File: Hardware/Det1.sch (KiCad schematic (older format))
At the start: 11 parts

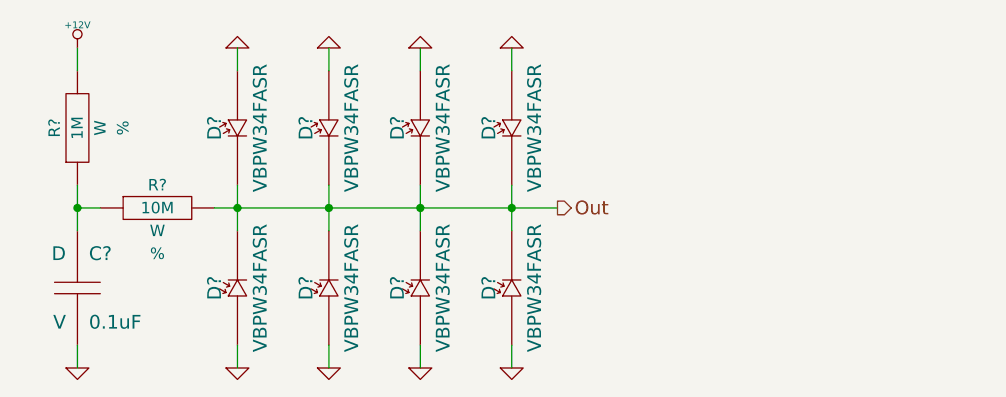
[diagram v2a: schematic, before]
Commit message: Fill BOM fields for detector section
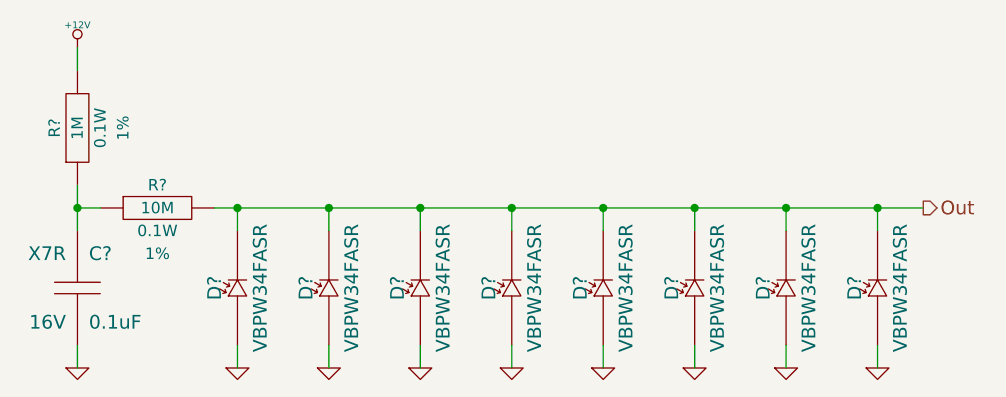
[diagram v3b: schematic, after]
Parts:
- removed C?: 0.1uF, ~, symbol C
- removed D? (x8): VBPW34FASR, ~, symbol DIODE-PHOTO
- removed R?: 10M, ~, symbol R
- added C?: 0.1uF, CAPC1608, symbol C
- added D? (x8): VBPW34FASR, DIOC-BPW34R, symbol DIODE-PHOTO
- added R?: 10M, RESC1608, symbol R
- R?: footprint ~ -> RESC1608; Distributor Part No (none) -> 311-1.00MHRCT-ND; MFR Name (none) -> Yageo; MFR Part No (none) -> RC0603FR-071ML; Power W -> 0.1W; Tolerance % -> 1%
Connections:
- net GND: now also C?.2, D?.1, D?.1, D?.1, D?.1, D?.1, D?.1, D?.1, D?.1
- net Out: now also D?.2, D?.2, D?.2, D?.2, D?.2, D?.2, D?.2, D?.2, R?.2
- net at R?.1: now also C?.1, R?.1

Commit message: Initial annotation
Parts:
- gave numbers to parts that had none: 11
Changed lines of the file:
@@
 $EndDescr
 $Comp
-L GND #PWR?
+L GND #PWR3
 U 1 1 523D026F
 P 3800 3700
-F 0 "#PWR?" H 3800 3700 30  0001 C CNN
+F 0 "#PWR3" H 3800 3700 30  0001 C CNN
 F 1 "GND" H 3800 3630 30  0001 C CNN
 F 2 "" H 3800 3700 60  0000 C CNN
@@
 $EndComp
 $Comp
-L GND #PWR?
+L GND #PWR4
 U 1 1 523D027E
 P 4200 3700
-F 0 "#PWR?" H 4200 3700 30  0001 C CNN
+F 0 "#PWR4" H 4200 3700 30  0001 C CNN
 F 1 "GND" H 4200 3630 30  0001 C CNN
 F 2 "" H 4200 3700 60  0000 C CNN
@@
 $EndComp
 $Comp
-L GND #PWR?
+L GND #PWR6
 U 1 1 523D029C
 P 5000 3700
-F 0 "#PWR?" H 5000 3700 30  0001 C CNN
+F 0 "#PWR6" H 5000 3700 30  0001 C CNN
 F 1 "GND" H 5000 3630 30  0001 C CNN
 F 2 "" H 5000 3700 60  0000 C CNN
@@
 $EndComp
 $Comp
-L GND #PWR?
+L GND #PWR5
 U 1 1 523D02AB
 P 4600 3700
-F 0 "#PWR?" H 4600 3700 30  0001 C CNN
+F 0 "#PWR5" H 4600 3700 30  0001 C CNN
 F 1 "GND" H 4600 3630 30  0001 C CNN
 F 2 "" H 4600 3700 60  0000 C CNN
@@
 Out
 $Comp
-L +12V #PWR?
+L +12V #PWR1
 U 1 1 523D1D05
 P 3100 2300
-F 0 "#PWR?" H 3100 2250 20  0001 C CNN
+F 0 "#PWR1" H 3100 2250 20  0001 C CNN
 F 1 "+12V" H 3100 2400 30  0000 C CNN
 F 2 "" H 3100 2300 60  0000 C CNN
@@
 $EndComp
 $Comp
-L R R?
+L R R1
 U 1 1 523D1D2F
 P 3100 2650
-F 0 "R?" H 3100 2750 50  0000 C CNN
+F 0 "R1" H 3100 2750 50  0000 C CNN
 F 1 "1M" H 3100 2650 50  0000 C CNN
 F 2 "RESC1608" H 3100 2650 60  0001 C CNN
@@
 $EndComp
 $Comp
-L GND #PWR?
+L GND #PWR2
 U 1 1 523D1DB5
 P 3100 3700
-F 0 "#PWR?" H 3100 3700 30  0001 C CNN
+F 0 "#PWR2" H 3100 3700 30  0001 C CNN
 F 1 "GND" H 3100 3630 30  0001 C CNN
 F 2 "" H 3100 3700 60  0000 C CNN
@@
 Connection ~ 3100 3000
 $Comp
-L DIODE-PHOTO D?
+L DIODE-PHOTO D8
 U 1 1 52411FCC
 P 6600 3350
-F 0 "D?" H 6600 3450 60  0000 C CNN
+F 0 "D8" H 6600 3450 60  0000 C CNN
 F 1 "VBPW34FASR" H 6600 3250 60  0000 C CNN
 F 2 "DIOC-BPW34R" H 6600 3350 60  0001 C CNN
@@
 $EndComp
 $Comp
-L GND #PWR?
+L GND #PWR7
 U 1 1 52411FD2
 P 5400 3700
-F 0 "#PWR?" H 5400 3700 30  0001 C CNN
+F 0 "#PWR7" H 5400 3700 30  0001 C CNN
 F 1 "GND" H 5400 3630 30  0001 C CNN
 F 2 "" H 5400 3700 60  0000 C CNN
@@
 $EndComp
 $Comp
-L GND #PWR?
+L GND #PWR8
 U 1 1 52411FD8
 P 5800 3700
-F 0 "#PWR?" H 5800 3700 30  0001 C CNN
+F 0 "#PWR8" H 5800 3700 30  0001 C CNN
 F 1 "GND" H 5800 3630 30  0001 C CNN
 F 2 "" H 5800 3700 60  0000 C CNN
@@
 $EndComp
 $Comp
-L GND #PWR?
+L GND #PWR10
 U 1 1 52411FDE
 P 6600 3700
-F 0 "#PWR?" H 6600 3700 30  0001 C CNN
+F 0 "#PWR10" H 6600 3700 30  0001 C CNN
 F 1 "GND" H 6600 3630 30  0001 C CNN
 F 2 "" H 6600 3700 60  0000 C CNN
@@
 $EndComp
 $Comp
-L GND #PWR?
+L GND #PWR9
 U 1 1 52411FE4
 P 6200 3700
-F 0 "#PWR?" H 6200 3700 30  0001 C CNN
+F 0 "#PWR9" H 6200 3700 30  0001 C CNN
 F 1 "GND" H 6200 3630 30  0001 C CNN
 F 2 "" H 6200 3700 60  0000 C CNN
@@
 Connection ~ 6600 3000
 $Comp
-L DIODE-PHOTO D?
+L DIODE-PHOTO D7
 U 1 1 52412B07
 P 6200 3350
-F 0 "D?" H 6200 3450 60  0000 C CNN
+F 0 "D7" H 6200 3450 60  0000 C CNN
 F 1 "VBPW34FASR" H 6200 3250 60  0000 C CNN
 F 2 "DIOC-BPW34R" H 6200 3350 60  0001 C CNN
@@
 $EndComp
 $Comp
-L DIODE-PHOTO D?
+L DIODE-PHOTO D6
 U 1 1 52412B10
 P 5800 3350
-F 0 "D?" H 5800 3450 60  0000 C CNN
+F 0 "D6" H 5800 3450 60  0000 C CNN
 F 1 "VBPW34FASR" H 5800 3250 60  0000 C CNN
 F 2 "DIOC-BPW34R" H 5800 3350 60  0001 C CNN
@@
 $EndComp
 $Comp
-L DIODE-PHOTO D?
+L DIODE-PHOTO D5
 U 1 1 52412B19
 P 5400 3350
-F 0 "D?" H 5400 3450 60  0000 C CNN
+F 0 "D5" H 5400 3450 60  0000 C CNN
 F 1 "VBPW34FASR" H 5400 3250 60  0000 C CNN
 F 2 "DIOC-BPW34R" H 5400 3350 60  0001 C CNN
@@
 $EndComp
 $Comp
-L DIODE-PHOTO D?
+L DIODE-PHOTO D4
 U 1 1 52412B22
 P 5000 3350
-F 0 "D?" H 5000 3450 60  0000 C CNN
+F 0 "D4" H 5000 3450 60  0000 C CNN
 F 1 "VBPW34FASR" H 5000 3250 60  0000 C CNN
 F 2 "DIOC-BPW34R" H 5000 3350 60  0001 C CNN
@@
 $EndComp
 $Comp
-L DIODE-PHOTO D?
+L DIODE-PHOTO D3
 U 1 1 52412B2B
 P 4600 3350
-F 0 "D?" H 4600 3450 60  0000 C CNN
+F 0 "D3" H 4600 3450 60  0000 C CNN
 F 1 "VBPW34FASR" H 4600 3250 60  0000 C CNN
 F 2 "DIOC-BPW34R" H 4600 3350 60  0001 C CNN
@@
 $EndComp
 $Comp
-L DIODE-PHOTO D?
+L DIODE-PHOTO D2
 U 1 1 52412B34
 P 4200 3350
-F 0 "D?" H 4200 3450 60  0000 C CNN
+F 0 "D2" H 4200 3450 60  0000 C CNN
 F 1 "VBPW34FASR" H 4200 3250 60  0000 C CNN
 F 2 "DIOC-BPW34R" H 4200 3350 60  0001 C CNN
@@
 $EndComp
 $Comp
-L DIODE-PHOTO D?
+L DIODE-PHOTO D1
 U 1 1 52412B3D
 P 3800 3350
-F 0 "D?" H 3800 3450 60  0000 C CNN
+F 0 "D1" H 3800 3450 60  0000 C CNN
 F 1 "VBPW34FASR" H 3800 3250 60  0000 C CNN
 F 2 "DIOC-BPW34R" H 3800 3350 60  0001 C CNN
@@
 $EndComp
 $Comp
-L R R?
+L R R2
 U 1 1 52412CA0
 P 3450 3000
-F 0 "R?" H 3450 3100 50  0000 C CNN
+F 0 "R2" H 3450 3100 50  0000 C CNN
 F 1 "10M" H 3450 3000 50  0000 C CNN
 F 2 "RESC1608" H 3450 3000 60  0001 C CNN
@@
 $EndComp
 $Comp
-L C C?
+L C C1
 U 1 1 52412D91
 P 3100 3350
-F 0 "C?" H 3150 3500 60  0000 L CNN
+F 0 "C1" H 3150 3500 60  0000 L CNN
 F 1 "0.1uF" H 3150 3200 60  0000 L CNN
 F 2 "CAPC1608" H 3100 3350 60  0001 C CNN
